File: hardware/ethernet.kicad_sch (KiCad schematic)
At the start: 13 parts, among them J4 HC-RJ45-055-7, U2 TMI7301

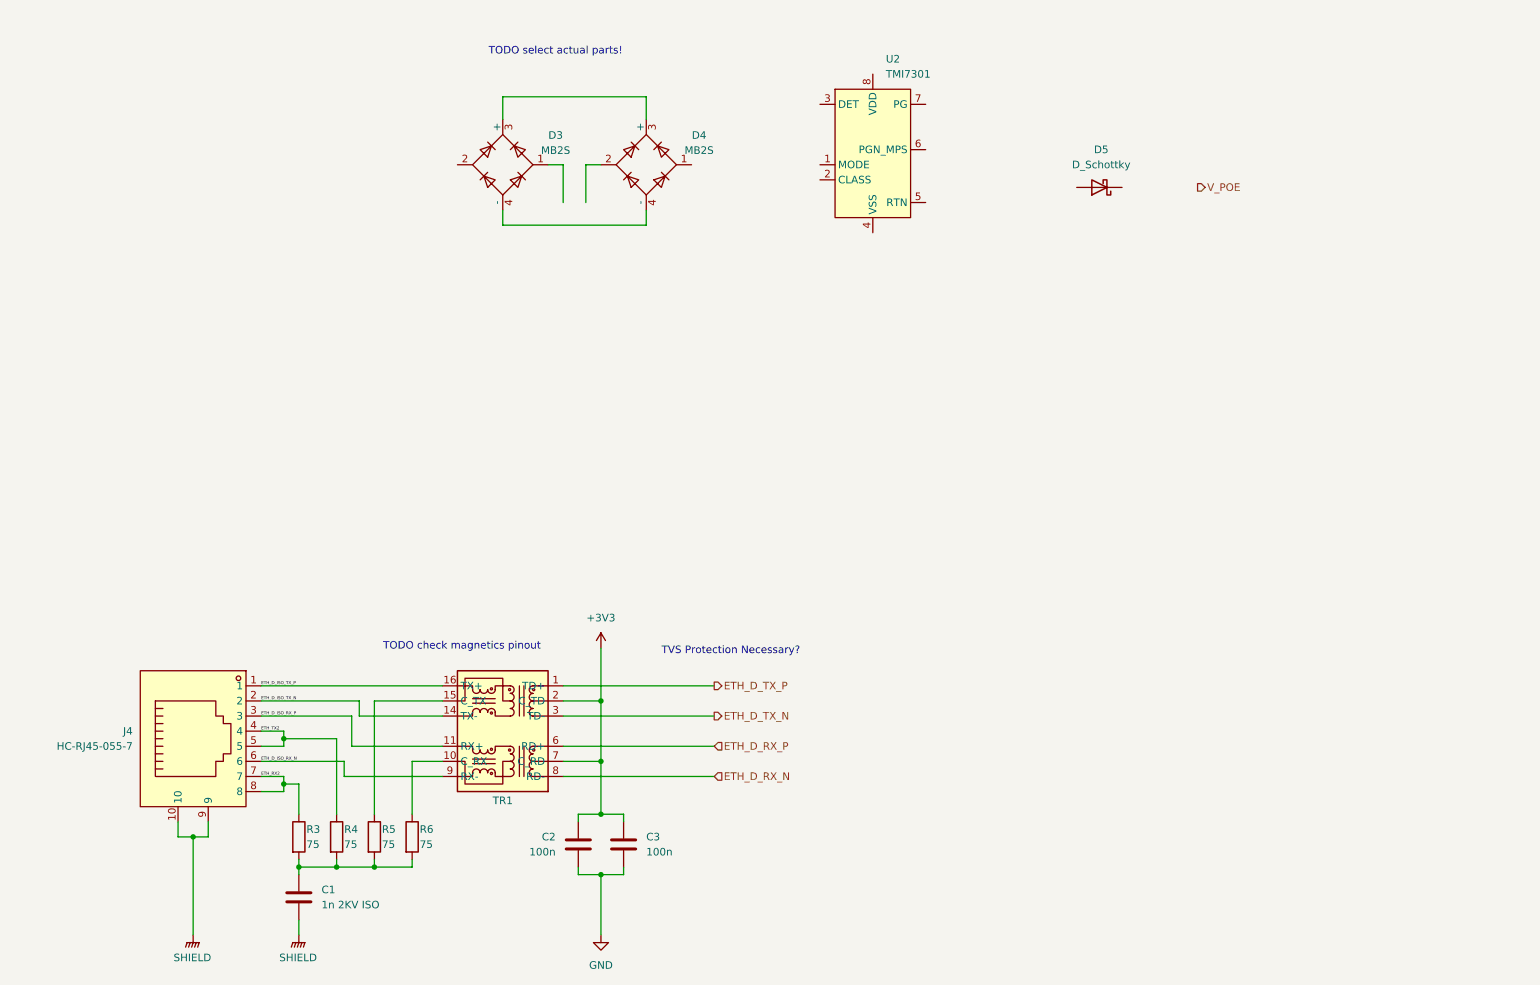
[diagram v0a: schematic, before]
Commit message: POE layout considerationa
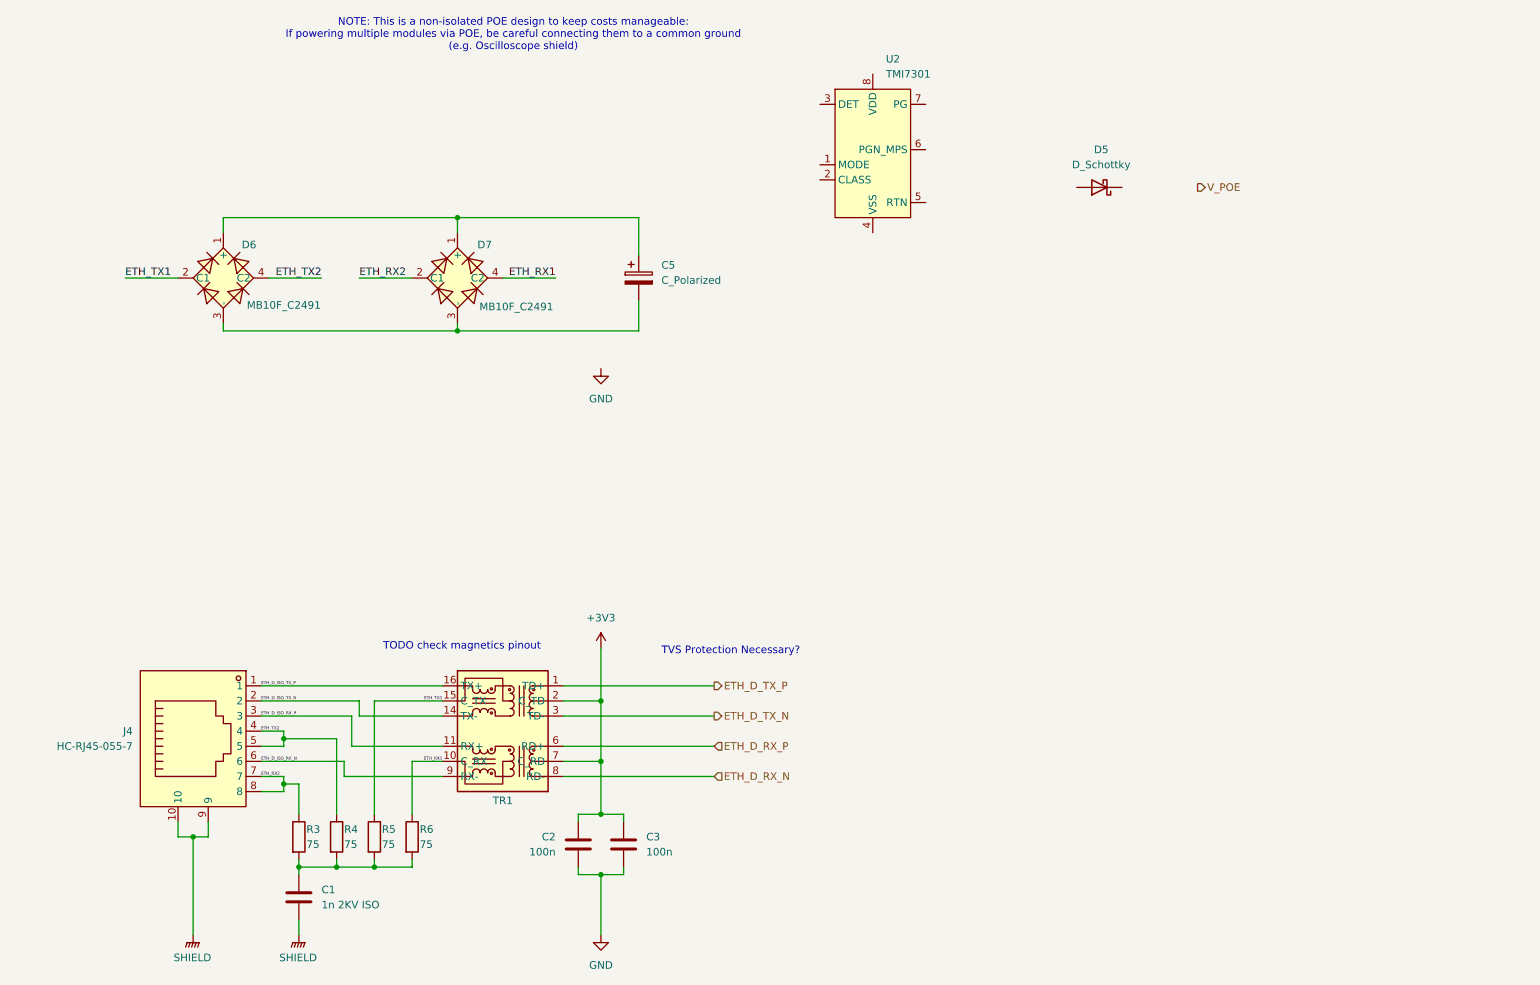
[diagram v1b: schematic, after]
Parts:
- removed D3, D4: MB2S, Package_TO_SOT_SMD:TO-269AA, symbol Diode_Bridge:MB2S
- added C5: C_Polarized, symbol Device:C_Polarized
- added D6, D7: MB10F_C2491, uPTP:DIO-BG-SMD_4P-L4.9-W4.0-P2.54-LS7.0-BR, symbol uPTP:MB10F_C2491
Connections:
- net ETH_RX2: now also D7.2 (C1)
- net ETH_TX2: now also D6.4 (C2)
- net ETH_RX1: now reaches R6.1, TR1.10 (C_RX)
- net ETH_RX1: now also D7.4 (C2)
- net ETH_TX1: now reaches R5.1, TR1.15 (C_TX)
- net ETH_TX1: now also D6.2 (C1)
- new net: C5.1, D6.1 (+), D7.1 (+)
- new net: C5.2, D6.3 (-), D7.3 (-)
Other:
- note added: "NOTE: This is a non-isolated POE design to keep costs manageable: If powering multiple modules via POE, be careful connecting them to a common ground (e.g. Oscilloscope shield)"
- note removed: "TODO select actual parts!"

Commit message: Vaguely convincing render...
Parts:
- added C5: 100n 100V/60V?, Capacitor_SMD:C_0805_2012Metric, symbol Device:C
- added D5: SMAJ58A, Diode_SMD:D_SMA, symbol Diode:SMAJ58A
- added JP2: SHIELD_BRIDGE, Jumper:SolderJumper-2_P1.3mm_Open_RoundedPad1.0x1.5mm, symbol Jumper:Jumper_2_Open
- added R11: 24.9k, Resistor_SMD:R_0402_1005Metric, symbol Device:R
- added R12: 1k, Resistor_SMD:R_0402_1005Metric, symbol Device:R
- added R13, R14, R15, R17: 49.9, Resistor_SMD:R_0402_1005Metric, symbol Device:R
- added R16: 100k, Resistor_SMD:R_0402_1005Metric, symbol Device:R
- renumbered C5 to 47u1, C1 to C2, C2 to C3, C3 to C4, D6 to D3, D7 to D4, D5 to D6, R6 to R10, R3 to R7, R4 to R8, R5 to R9
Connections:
- net GND: now also 47u1.2, U2.5 (RTN), JP2.2 (B)
- net SHIELD: now also JP2.1 (A)
- net V_POE: now also D6.1 (K)
- net ETH_BOB_SMITH: now reaches C2.1, R10.2, R7.2, R8.2, R9.2
- net ETH_POE_P: now reaches 47u1.1, D3.1 (+), D4.1 (+)
- net ETH_POE_P: now also D6.2 (A), U2.8 (VDD), C5.1, D5.1 (A1), R11.1, R16.1
- net ETH_POE_N: now reaches D3.3 (-), D4.3 (-)
- net ETH_POE_N: now also U2.1 (MODE), U2.4 (VSS), C5.2, D5.2 (A2), R12.2; no longer 47u1.2
- net ETH_POE_CLASS: now reaches U2.2 (CLASS)
- net ETH_POE_CLASS: now also R12.1
- net ETH_POE_DET: now reaches U2.3 (DET)
- net ETH_POE_DET: now also R11.2
- net POE_READY: now reaches U2.6 (PGN_MPS)
- net POE_READY: now also R16.2
- no-connect marks 0 -> 1
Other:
- note added: "Classification Class 1 (<4W)"
- note added: "POE Cable side is floating when no POE present"
- note added: "TVS Protection Necessary? RECOMMENDED FOR POE DESIGNS"
- note added: "Unsure if Phy has built-in termination, placeholders close to MCU"
- note removed: "TVS Protection Necessary?"
- moved on the sheet: 47u1, D3, D4, D6, U2

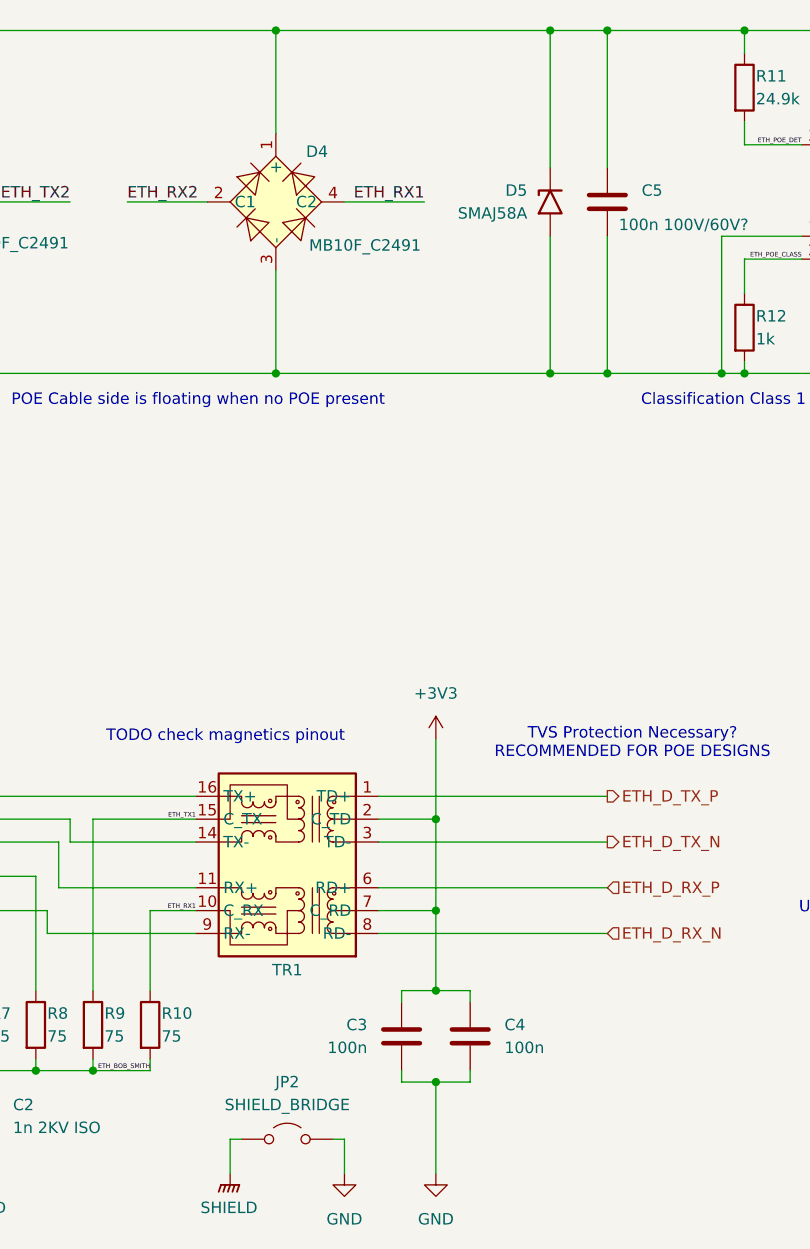
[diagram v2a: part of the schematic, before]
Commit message: Prep for change to SI3404 https://www.skyworksinc.com/-/media/Skyworks/SL/documents/public/application-notes/an1130-si3404-06x-dg.pdf
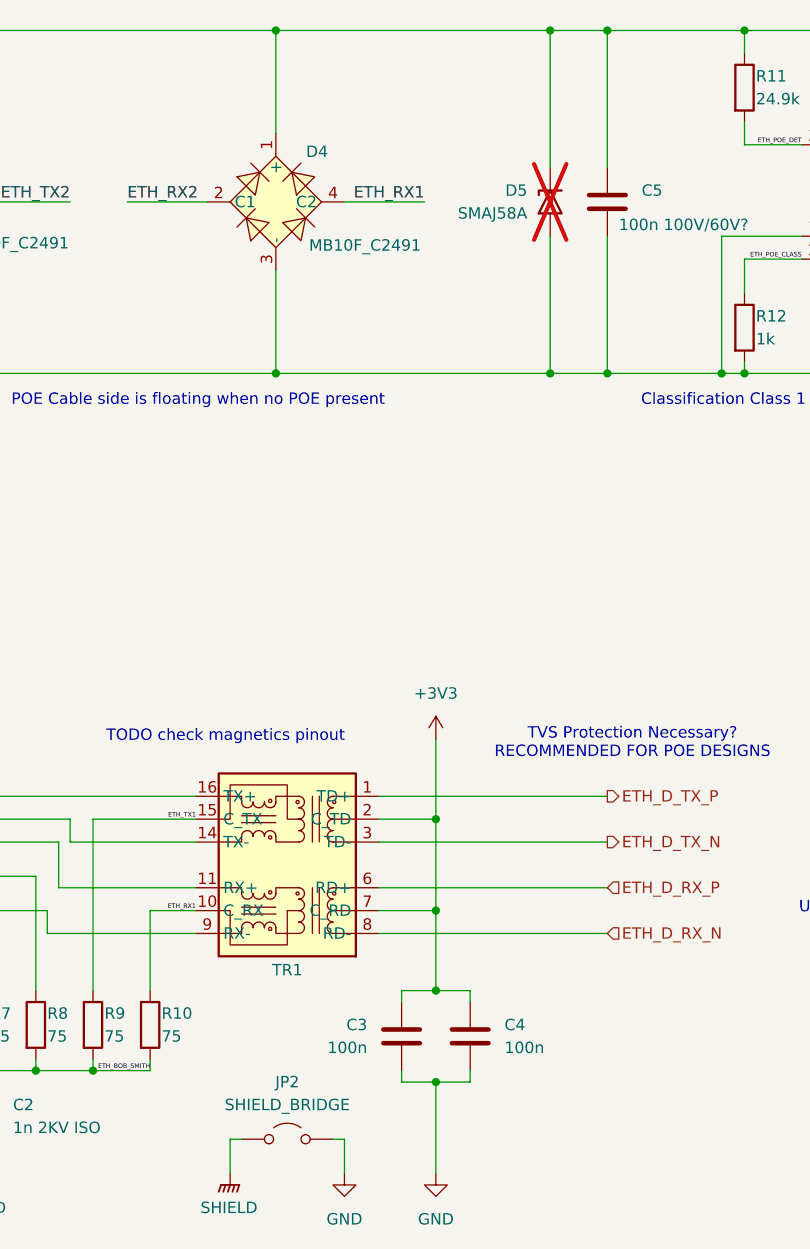
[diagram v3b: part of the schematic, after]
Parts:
- D5: now not fitted
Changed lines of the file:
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@@
 (kicad_sch
-	(version 20231120)
+	(version 20250114)
 	(generator "eeschema")
-	(generator_version "8.0")
+	(generator_version "9.0")
 	(paper "A4")
+	(text "POE Cable side is floating when no POE present"
+		(exclude_from_sim no)
+		(at 94.234 85.598 0)
+		(effects
+			(font
+				(size 1.27 1.27)
+			)
+		)
+	)
+	(text "TVS Protection Necessary?\nRECOMMENDED FOR POE DESIGNS"
+		(exclude_from_sim no)
+		(at 142.494 123.698 0)
+		(effects
+			(font
+				(size 1.27 1.27)
+			)
+		)
+	)
+	(text "Classification Class 1 (<4W)"
+		(exclude_from_sim no)
+		(at 155.702 85.598 0)
+		(effects
+			(font
+				(size 1.27 1.27)
+			)
+		)
+	)
+	(text "TODO check magnetics pinout"
+		(exclude_from_sim no)
+		(at 97.282 122.936 0)
+		(effects
+			(font
+				(size 1.27 1.27)
+			)
+		)
+	)
+	(text "NOTE: This is a non-isolated POE design to keep costs manageable:\nIf powering multiple modules via POE, be careful connecting them to a common ground\n(e.g. Oscilloscope shield)"
+		(exclude_from_sim no)
+		(at 136.652 32.766 0)
+		(effects
+			(font
+				(size 1.27 1.27)
+			)
+		)
+	)
+	(text "Unsure if Phy has built-in termination,\nplaceholders close to MCU"
+		(exclude_from_sim no)
+		(at 177.546 143.002 0)
+		(effects
+			(font
+				(size 1.27 1.27)
+			)
+		)
+	)
 	(junction
 		(at 67.31 146.05)
@@
 		)
 	)
-	(text "POE Cable side is floating when no POE present"
-		(exclude_from_sim no)
-		(at 94.234 85.598 0)
-		(effects
-			(font
-				(size 1.27 1.27)
-			)
-		)
-	)
-	(text "TVS Protection Necessary?\nRECOMMENDED FOR POE DESIGNS"
-		(exclude_from_sim no)
-		(at 142.494 123.698 0)
-		(effects
-			(font
-				(size 1.27 1.27)
-			)
-		)
-	)
-	(text "Classification Class 1 (<4W)"
-		(exclude_from_sim no)
-		(at 155.702 85.598 0)
-		(effects
-			(font
-				(size 1.27 1.27)
-			)
-		)
-	)
-	(text "TODO check magnetics pinout"
-		(exclude_from_sim no)
-		(at 97.282 122.936 0)
-		(effects
-			(font
-				(size 1.27 1.27)
-			)
-		)
-	)
-	(text "NOTE: This is a non-isolated POE design to keep costs manageable:\nIf powering multiple modules via POE, be careful connecting them to a common ground\n(e.g. Oscilloscope shield)"
-		(exclude_from_sim no)
-		(at 136.652 32.766 0)
-		(effects
-			(font
-				(size 1.27 1.27)
-			)
-		)
-	)
-	(text "Unsure if Phy has built-in termination,\nplaceholders close to MCU"
-		(exclude_from_sim no)
-		(at 177.546 143.002 0)
-		(effects
-			(font
-				(size 1.27 1.27)
-			)
-		)
-	)
 	(label "ETH_POE_N"
 		(at 64.77 82.55 0)
-		(fields_autoplaced yes)
 		(effects
 			(font
@@
 	(label "ETH_RX1"
 		(at 93.98 142.24 180)
-		(fields_autoplaced yes)
 		(effects
 			(font
@@
 	(label "ETH_D_ISO_TX_P"
 		(at 63.5 129.54 0)
-		(fields_autoplaced yes)
 		(effects
 			(font
@@
 	(label "ETH_POE_P"
 		(at 66.04 44.45 0)
-		(fields_autoplaced yes)
 		(effects
 			(font
@@
 	(label "ETH_RX1"
 		(at 119.38 63.5 180)
-		(fields_autoplaced yes)
 		(effects
 			(font
@@
 	(label "ETH_D_ISO_RX_P"
 		(at 63.5 134.62 0)
-		(fields_autoplaced yes)
 		(effects
 			(font
@@
 	(label "ETH_POE_DET"
 		(at 161.29 57.15 180)
-		(fields_autoplaced yes)
 		(effects
 			(font
@@
 	(label "ETH_RX2"
 		(at 63.5 144.78 0)
-		(fields_autoplaced yes)
 		(effects
 			(font
@@
 	(label "ETH_TX1"
 		(at 46.99 63.5 0)
-		(fields_autoplaced yes)
 		(effects
 			(font
@@
 	(label "ETH_TX1"
 		(at 93.98 132.08 180)
-		(fields_autoplaced yes)
 		(effects
 			(font
@@
 	(label "ETH_RX2"
 		(at 86.36 63.5 0)
-		(fields_autoplaced yes)
 		(effects
 			(font
@@
 	(label "ETH_TX2"
 		(at 63.5 137.16 0)
-		(fields_autoplaced yes)
 		(effects
 			(font
@@
 	(label "ETH_D_ISO_TX_N"
 		(at 63.5 132.08 0)
-		(fields_autoplaced yes)
 		(effects
 			(font
@@
 	(label "ETH_TX2"
 		(at 80.01 63.5 180)
-		(fields_autoplaced yes)
 		(effects
 			(font
@@
 	(label "ETH_POE_CLASS"
 		(at 161.29 69.85 180)
-		(fields_autoplaced yes)
 		(effects
 			(font
@@
 	(label "ETH_BOB_SMITH"
 		(at 88.9 160.02 180)
-		(fields_autoplaced yes)
 		(effects
 			(font
@@
 	(label "ETH_D_ISO_RX_N"
 		(at 63.5 142.24 0)
-		(fields_autoplaced yes)
 		(effects
 			(font
@@
 		(shape output)
 		(at 139.7 129.54 0)
-		(fields_autoplaced yes)
 		(effects
 			(font
@@
 		(shape output)
 		(at 222.25 64.77 0)
-		(fields_autoplaced yes)
 		(effects
 			(font
@@
 		(shape input)
 		(at 139.7 139.7 0)
-		(fields_autoplaced yes)
 		(effects
 			(font
@@
 		(shape input)
 		(at 139.7 144.78 0)
-		(fields_autoplaced yes)
 		(effects
 			(font
@@
 		(shape output)
 		(at 139.7 134.62 0)
-		(fields_autoplaced yes)
 		(effects
 			(font
@@
 		(shape output)
 		(at 222.25 44.45 0)
-		(fields_autoplaced yes)
 		(effects
 			(font
@@
 		(in_bom yes)
 		(on_board yes)
-		(dnp no)
+		(dnp yes)
 		(property "Reference" "D5"
 			(at 130.81 62.2299 90)

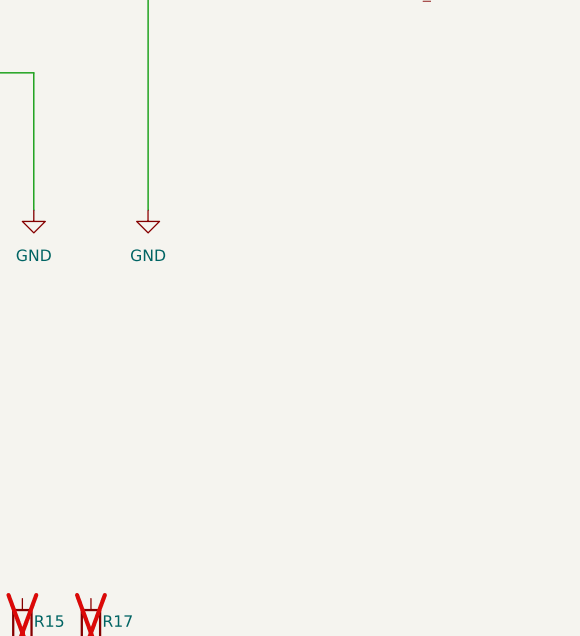
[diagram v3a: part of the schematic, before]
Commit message: Add SI3404 part
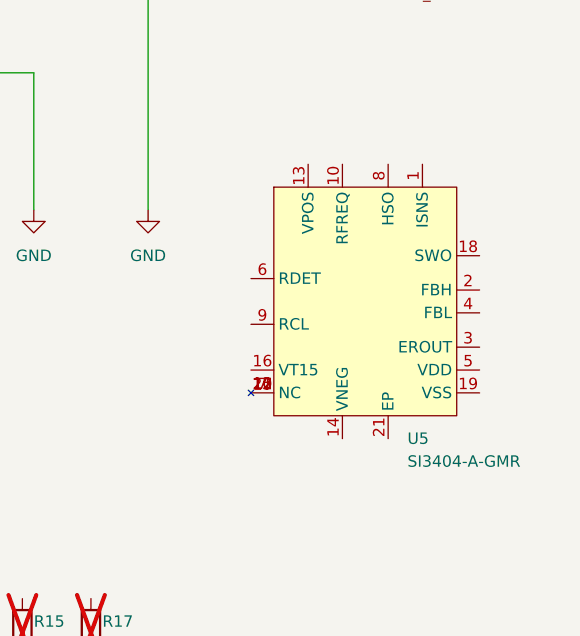
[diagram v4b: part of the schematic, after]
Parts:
- added U5: SI3404-A-GMR, Package_DFN_QFN:QFN-20-1EP_4x4mm_P0.5mm_EP2.6x2.6mm, symbol uPTP:SI3404-A-GMR
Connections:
- new net: U5.11 (NC), U5.12 (NC), U5.15 (NC), U5.17 (NC), U5.20 (NC), U5.7 (NC)
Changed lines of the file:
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@@
+		)
+	)
+	(symbol
+		(lib_id "uPTP:SI3404-A-GMR")
+		(at 220.98 99.06 0)
+		(unit 1)
+		(exclude_from_sim no)
+		(in_bom yes)
+		(on_board yes)
+		(dnp no)
+		(fields_autoplaced yes)
+		(property "Reference" "U5"
+			(at 225.6633 114.3 0)
+			(effects
+				(font
+					(size 1.27 1.27)
+				)
+				(justify left)
+			)
+		)
+		(property "Value" "SI3404-A-GMR"
+			(at 225.6633 116.84 0)
+			(effects
+				(font
+					(size 1.27 1.27)
+				)
+				(justify left)
+			)
+		)
+		(property "Footprint" "Package_DFN_QFN:QFN-20-1EP_4x4mm_P0.5mm_EP2.6x2.6mm"
+			(at 220.98 124.46 0)
+			(effects
+				(font
+					(size 1.27 1.27)
+				)
+				(hide yes)
+			)
+		)
+		(property "Datasheet" ""
+			(at 220.98 99.06 0)
+			(effects
+				(font
+					(size 1.27 1.27)
+				)
+				(hide yes)
+			)
+		)
+		(property "Description" "POE PD Controller"
+			(at 220.98 99.06 0)
+			(effects
+				(font
+					(size 1.27 1.27)
+				)
+				(hide yes)
+			)
+		)
+		(property "LCSC Part" "C461934"
+			(at 220.98 127 0)
+			(effects
+				(font
+					(size 1.27 1.27)
+				)
+				(hide yes)
+			)
+		)
+		(pin "3"
+		)
+		(pin "11"
+		)
+		(pin "6"
+		)
+		(pin "9"
+		)
+		(pin "17"
+		)
+		(pin "16"
+		)
+		(pin "13"
+		)
+		(pin "7"
+		)
+		(pin "12"
+		)
+		(pin "19"
+		)
+		(pin "8"
+		)
+		(pin "4"
+		)
+		(pin "20"
+		)
+		(pin "1"
+		)
+		(pin "18"
+		)
+		(pin "15"
+		)
+		(pin "10"
+		)
+		(pin "21"
+		)
+		(pin "5"
+		)
+		(pin "14"
+		)
+		(pin "2"
+		)
+		(instances
+			(project ""
+				(path "/c29659fd-9e8d-4714-a690-4e74e6e849c2/8e64a963-7181-4c69-8059-c99395347002"
+					(reference "U5")
+					(unit 1)
+				)
+			)
 		)
 	)
